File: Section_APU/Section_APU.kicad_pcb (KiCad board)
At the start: 2 copper layers, 39 x 79.5 mm, 24 parts, among them J1 APU ribbon, J2 Backlight, SW1 APU MASTER SW, SW2 APU START

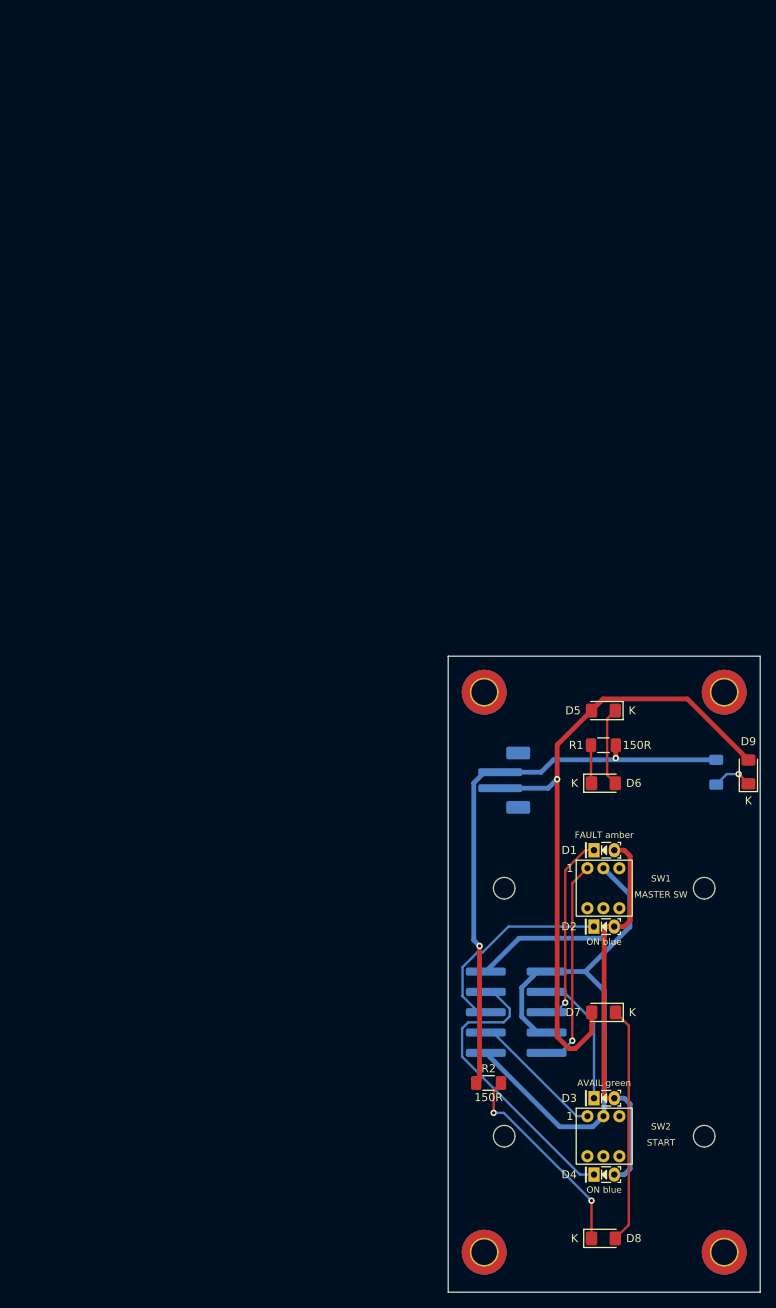
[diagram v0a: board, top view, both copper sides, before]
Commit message: Tidy the APU schematic and put the board on its sheet
Schematic: parts in spaced groups on the 100 mil grid, reference and value
outside the symbol body, horizontal on rotated parts, and GND on sideways
pins as a label instead of a power symbol that crowded its neighbours.

PCB: moved by (-54, -80) mm onto the middle of the A4 sheet, grid origin at
v1's (0, 0), title block filled in. Rerouted: ERC 0, DRC 0, nothing
unconnected, no schematic-parity issues.

Co-Authored-By: Claude Opus 5.5 <noreply@anthropic.com>
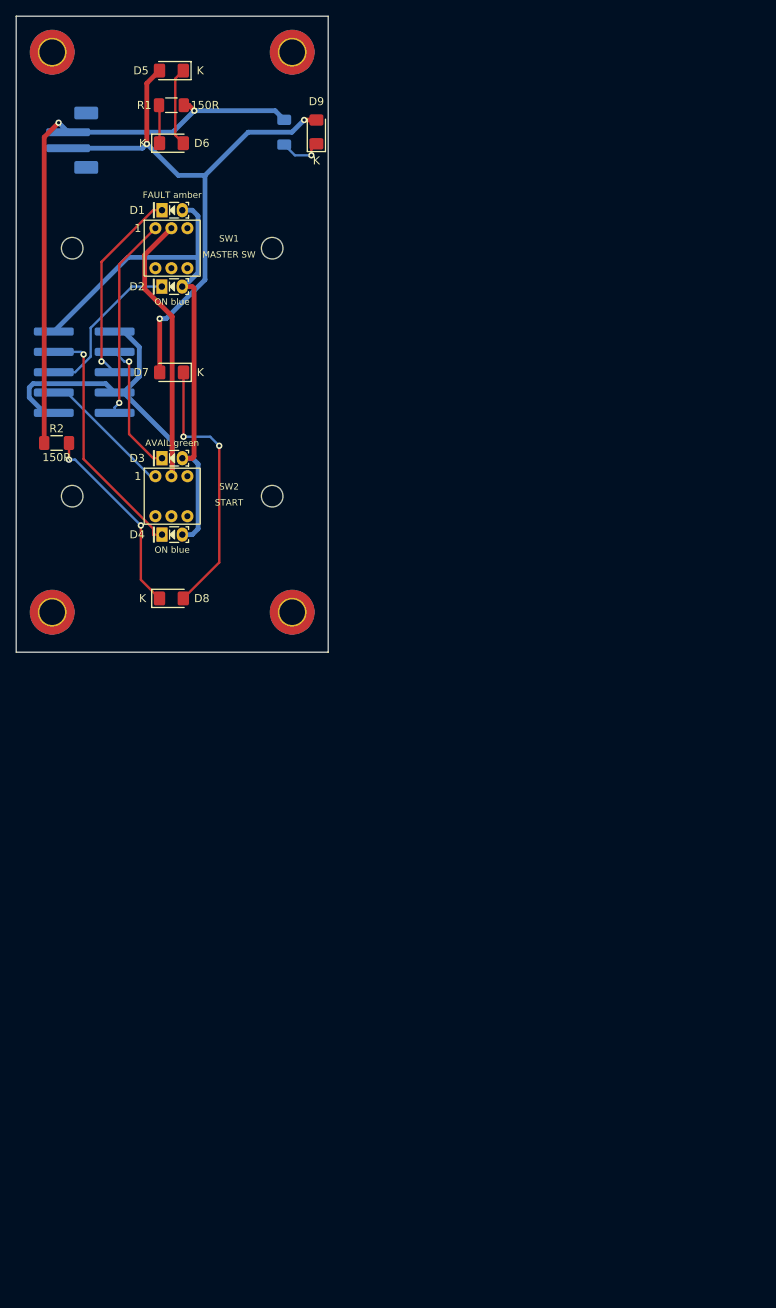
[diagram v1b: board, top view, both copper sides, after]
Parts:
- moved D2 96.5 mm to (146.7, 99.3)
- moved D5 96.5 mm to (147.9, 72.3)
- moved D1 96.5 mm to (146.7, 89.8)
- moved D3 96.5 mm to (146.7, 120.8)
- moved D4 96.5 mm to (146.7, 130.3)
- moved D6 96.5 mm to (147.9, 81.4)
- moved D7 96.5 mm to (147.9, 110.0)
- moved D8 96.5 mm to (147.9, 138.3)
- moved D9 96.5 mm to (166.0, 80.0)
- moved H1 96.5 mm to (133.0, 70.0)
- moved H2 96.5 mm to (163.0, 70.0)
- moved H3 96.5 mm to (133.0, 140.0)
- moved H4 96.5 mm to (163.0, 140.0)
- moved H5 96.5 mm to (135.5, 94.5)
- moved H6 96.5 mm to (160.5, 94.5)
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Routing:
- net +9V_BL: track 81.8 -> 73.0 mm, vias 1 -> 3
- net LED_APU_START_ON: track 37.5 -> 31.1 mm, vias 0 -> 1
- net LED_APU_MASTER_ON: track 25.9 -> 20.0 mm
- net BL2_MID: track 29.6 -> 33.9 mm, vias 0 -> 2
- net GND: track 71.1 -> 74.8 mm
- net +5V_LED: track 68.3 -> 70.7 mm
- net BL_RET: track 71.3 -> 72.6 mm
- net BL2_R: track 25.6 -> 24.6 mm
- net APU_MASTER_SW: track 26.2 -> 25.2 mm
- net LED_APU_MASTER_FAULT: track 24.0 -> 24.9 mm
- net BL3_R: track 5.07 -> 5.65 mm
- net LED_APU_AVAIL: track 17.0 -> 16.7 mm, vias 0 -> 1

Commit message: Single-LED backlight strings on 330 ohm, not 470
A pair of backlight LEDs on 150 ohm runs at 17 mA (Stefano's figure). The
470 ohm came from an estimated 11 mA per string, which was wrong. For the
same 17 mA a single LED needs V / (2 I) + 75 ohm = 330 ohm. Changed on APU
(R3), GPWS (R5), AIR COND (R7, the v1 R76) and EXT LT (R16); the document's
backlight currents now use 17 mA, ~1.1 A in all. The four boards rebuilt
and rerouted: ERC 0, DRC 0, nothing unconnected, no parity issues.

Co-Authored-By: Claude Opus 5.5 <noreply@anthropic.com>
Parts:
- R3: value 470 -> 330
